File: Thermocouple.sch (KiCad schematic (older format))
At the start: 22 parts, among them P2 CONN_3X2, P3 CONN_2, U2 MCP3901, U3 LMT84, U4 OPA4170

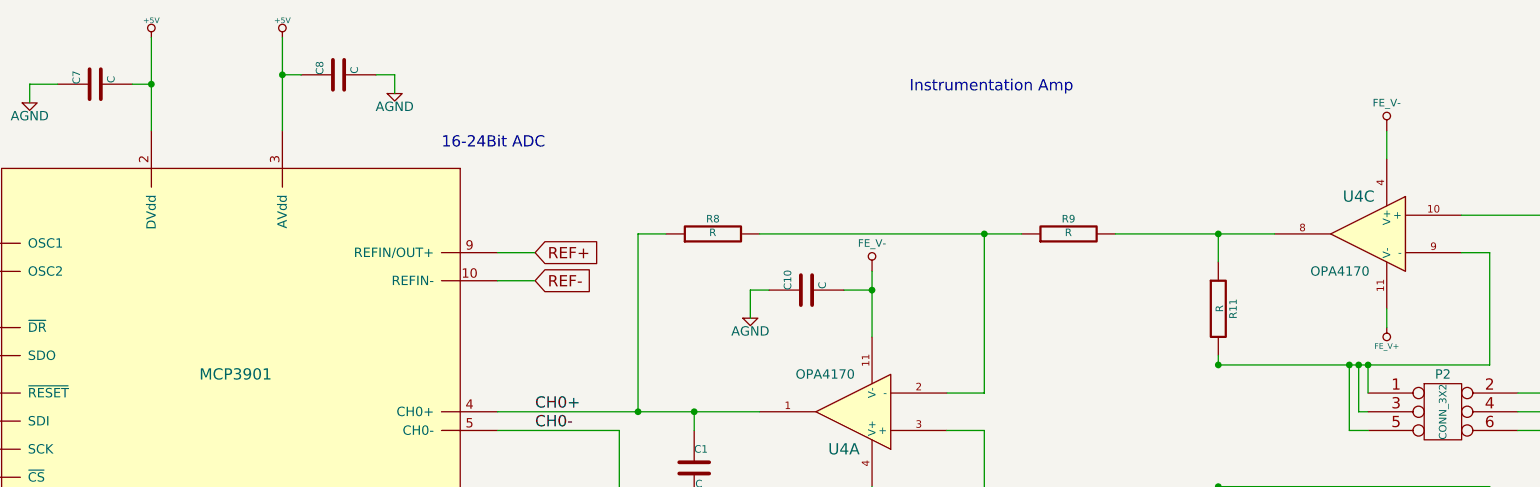
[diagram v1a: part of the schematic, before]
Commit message: Layout Work Session 12
Pulled from CE.

Session 11 missed due to corrupted pcb file pulled from CE
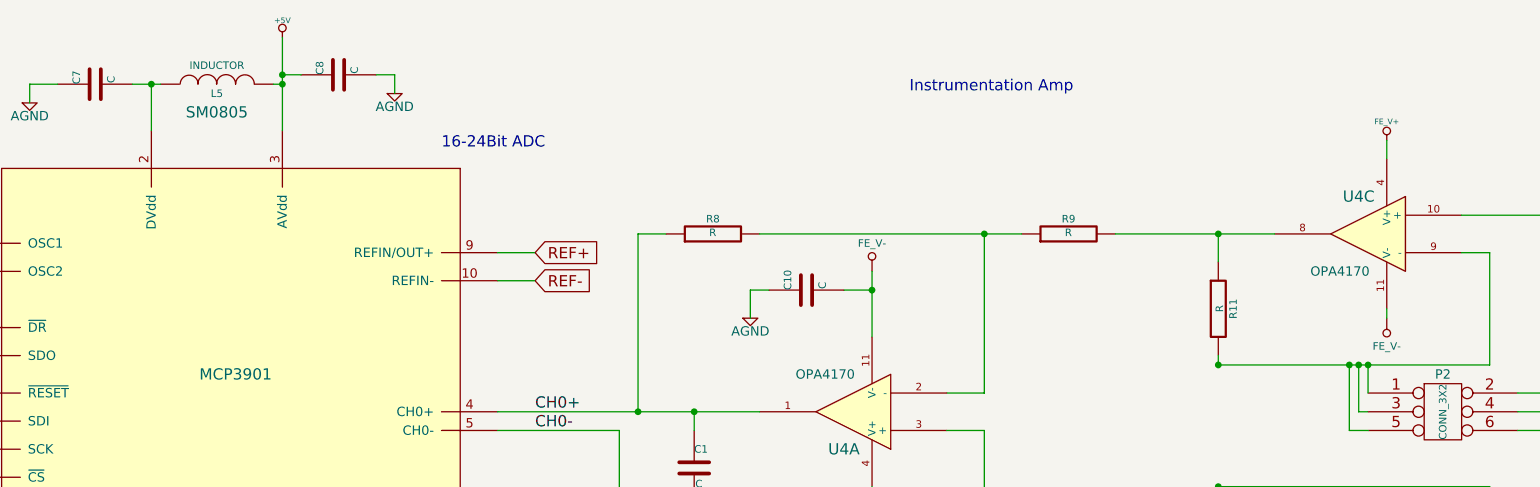
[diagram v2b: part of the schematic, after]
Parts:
- added L5: INDUCTOR, SM0805, symbol INDUCTOR
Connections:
- net +5V: now also L5.2; no longer C7.2, U2.2 (DVdd)
- net FE_V+: now also U4.4 (V+); no longer U4.11 (V-)
- net FE_V-: now also U4.11 (V-); no longer U4.4 (V+)
- new net: C7.2, L5.1, U2.2 (DVdd)
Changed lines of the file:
@@
-EESchema Schematic File Version 2
+EESchema Schematic File Version 2  date 11/21/2013 11:46:41 PM
 LIBS:power
 LIBS:device
@@
 LIBS:BenchBuddy
 LIBS:BenchBuddy-cache
-EELAYER 24 0
+EELAYER 27 0
 EELAYER END
 $Descr A4 11693 8268
@@
 Sheet 2 9
 Title ""
-Date "13 nov 2013"
+Date "22 nov 2013"
 Rev ""
 Comp ""
@@
 	6250 2550 6250 2900
 Wire Wire Line
-	9000 2750 9000 2850
-Wire Wire Line
 	6250 3700 6250 3850
-Wire Wire Line
-	9000 1800 9000 1950
 Wire Wire Line
 	9000 5000 9000 4850
@@
 $EndComp
 Wire Wire Line
-	2400 1300 2400 1800
-Wire Wire Line
-	2400 1550 2300 1550
+	2300 1550 2450 1550
 Connection ~ 2400 1550
 Wire Wire Line
@@
 Wire Wire Line
 	3100 4600 3100 4850
-$Comp
-L +5V #PWR04
-U 1 1 5257AAC2
-P 2400 1300
-F 0 "#PWR04" H 2400 1390 20  0001 C CNN
-F 1 "+5V" H 2400 1390 30  0000 C CNN
-F 2 "~" H 2400 1300 60  0000 C CNN
-F 3 "~" H 2400 1300 60  0000 C CNN
-	1    2400 1300
-	1    0    0    -1
-$EndComp
 Text Notes 6500 6050 0    60   ~ 0
 TEMP SENSOR
@@
 	4550 3900 4550 6050
 $Comp
-L FE_V- #PWR13
+L FE_V- #PWR12
 U 1 1 526E01DB
 P 6250 2550
-F 0 "#PWR13" H 6250 2750 40  0001 C CNN
+F 0 "#PWR12" H 6250 2750 40  0001 C CNN
 F 1 "FE_V-" H 6250 2700 40  0000 C CNN
 F 2 "~" H 6250 2550 60  0000 C CNN
@@
 $EndComp
 $Comp
-L FE_V+ #PWR05
+L FE_V+ #PWR04
 U 1 1 526E01E1
 P 6250 3850
-F 0 "#PWR05" H 6250 3950 30  0001 C CNN
+F 0 "#PWR04" H 6250 3950 30  0001 C CNN
 F 1 "FE_V+" H 6250 3950 30  0000 C CNN
 F 2 "~" H 6250 3850 60  0000 C CNN
@@
 $EndComp
 $Comp
-L FE_V+ #PWR06
+L FE_V+ #PWR05
 U 1 1 526E01F1
 P 9000 5000
-F 0 "#PWR06" H 9000 5100 30  0001 C CNN
+F 0 "#PWR05" H 9000 5100 30  0001 C CNN
 F 1 "FE_V+" H 9000 5100 30  0000 C CNN
 F 2 "~" H 9000 5000 60  0000 C CNN
@@
 $EndComp
 $Comp
-L FE_V- #PWR17
+L FE_V- #PWR16
 U 1 1 526E0201
 P 9000 3950
-F 0 "#PWR17" H 9000 4150 40  0001 C CNN
+F 0 "#PWR16" H 9000 4150 40  0001 C CNN
 F 1 "FE_V-" H 9000 4100 40  0000 C CNN
 F 2 "~" H 9000 3950 60  0000 C CNN
@@
 L FE_V- #PWR15
 U 1 1 526E0207
-P 9000 1800
-F 0 "#PWR15" H 9000 2000 40  0001 C CNN
-F 1 "FE_V-" H 9000 1950 40  0000 C CNN
-F 2 "~" H 9000 1800 60  0000 C CNN
-F 3 "~" H 9000 1800 60  0000 C CNN
-	1    9000 1800
-	1    0    0    -1
-$EndComp
-$Comp
-L FE_V+ #PWR07
+P 9000 2800
+F 0 "#PWR15" H 9000 3000 40  0001 C CNN
+F 1 "FE_V-" H 9000 2950 40  0000 C CNN
+F 2 "~" H 9000 2800 60  0000 C CNN
+F 3 "~" H 9000 2800 60  0000 C CNN
+	1    9000 2800
+	-1   0    0    1
+$EndComp
+$Comp
+L FE_V+ #PWR06
 U 1 1 526E020D
-P 9000 2850
-F 0 "#PWR07" H 9000 2950 30  0001 C CNN
-F 1 "FE_V+" H 9000 2950 30  0000 C CNN
-F 2 "~" H 9000 2850 60  0000 C CNN
-F 3 "~" H 9000 2850 60  0000 C CNN
-	1    9000 2850
-	-1   0    0    1
-$EndComp
-$Comp
-L AGND #PWR08
+P 9000 1850
+F 0 "#PWR06" H 9000 1950 30  0001 C CNN
+F 1 "FE_V+" H 9000 1950 30  0000 C CNN
+F 2 "~" H 9000 1850 60  0000 C CNN
+F 3 "~" H 9000 1850 60  0000 C CNN
+	1    9000 1850
+	1    0    0    -1
+$EndComp
+$Comp
+L AGND #PWR07
 U 1 1 527EEF67
 P 3100 4850
-F 0 "#PWR08" H 3100 4850 40  0001 C CNN
+F 0 "#PWR07" H 3100 4850 40  0001 C CNN
 F 1 "AGND" H 3100 4780 50  0000 C CNN
 F 2 "~" H 3100 4850 60  0000 C CNN
@@
 $EndComp
 $Comp
-L AGND #PWR09
+L AGND #PWR08
 U 1 1 527EEF6D
 P 2300 4850
-F 0 "#PWR09" H 2300 4850 40  0001 C CNN
+F 0 "#PWR08" H 2300 4850 40  0001 C CNN
 F 1 "AGND" H 2300 4780 50  0000 C CNN
 F 2 "~" H 2300 4850 60  0000 C CNN
@@
 $EndComp
 $Comp
-L AGND #PWR010
+L AGND #PWR09
 U 1 1 527EEF73
 P 1750 1650
-F 0 "#PWR010" H 1750 1650 40  0001 C CNN
+F 0 "#PWR09" H 1750 1650 40  0001 C CNN
 F 1 "AGND" H 1750 1580 50  0000 C CNN
 F 2 "~" H 1750 1650 60  0000 C CNN
@@
 $EndComp
 $Comp
-L AGND #PWR011
+L AGND #PWR010
 U 1 1 527EEF79
 P 3700 1600
-F 0 "#PWR011" H 3700 1600 40  0001 C CNN
+F 0 "#PWR010" H 3700 1600 40  0001 C CNN
 F 1 "AGND" H 3700 1530 50  0000 C CNN
 F 2 "~" H 3700 1600 60  0000 C CNN
@@
 $EndComp
 $Comp
-L AGND #PWR012
+L AGND #PWR011
 U 1 1 527EEF7F
 P 5600 2800
-F 0 "#PWR012" H 5600 2800 40  0001 C CNN
+F 0 "#PWR011" H 5600 2800 40  0001 C CNN
 F 1 "AGND" H 5600 2730 50  0000 C CNN
 F 2 "~" H 5600 2800 60  0000 C CNN
@@
 $EndComp
 $Comp
-L AGND #PWR013
+L AGND #PWR012
 U 1 1 527EEF85
 P 5550 4000
-F 0 "#PWR013" H 5550 4000 40  0001 C CNN
+F 0 "#PWR012" H 5550 4000 40  0001 C CNN
 F 1 "AGND" H 5550 3930 50  0000 C CNN
 F 2 "~" H 5550 4000 60  0000 C CNN
@@
 $EndComp
 $Comp
-L AGND #PWR014
+L AGND #PWR013
 U 1 1 527EEF8B
 P 4900 4700
-F 0 "#PWR014" H 4900 4700 40  0001 C CNN
+F 0 "#PWR013" H 4900 4700 40  0001 C CNN
 F 1 "AGND" H 4900 4630 50  0000 C CNN
 F 2 "~" H 4900 4700 60  0000 C CNN
@@
 $EndComp
 $Comp
-L AGND #PWR015
+L AGND #PWR014
 U 1 1 527EEF91
 P 4800 6900
-F 0 "#PWR015" H 4800 6900 40  0001 C CNN
+F 0 "#PWR014" H 4800 6900 40  0001 C CNN
 F 1 "AGND" H 4800 6830 50  0000 C CNN
 F 2 "~" H 4800 6900 60  0000 C CNN
@@
 	1    0    0    -1
 $EndComp
+Wire Wire Line
+	9000 2800 9000 2750
+Wire Wire Line
+	9000 1850 9000 1950
+Wire Wire Line
+	2400 1550 2400 1800
+$Comp
+L INDUCTOR L5
+U 1 1 528976A6
+P 2750 1550
+F 0 "L5" V 2700 1550 40  0000 C CNN
+F 1 "INDUCTOR" V 2850 1550 40  0000 C CNN
+F 2 "SM0805" V 2600 1550 60  0000 C CNN
+F 3 "~" H 2750 1550 60  0000 C CNN
+	1    2750 1550
+	0    -1   -1   0
+$EndComp
+Wire Wire Line
+	3050 1550 3100 1550
+Connection ~ 3100 1550
 $EndSCHEMATC

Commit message: Layout Work Session 14
Pulled from CE
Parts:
- added C30, C31: C, SM0805, symbol C
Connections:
- net at U2.15 (OSC1): now also C30.2
- net at U2.16 (OSC2): now also C30.1
- net REF+: no longer names the net of U2.9 (REFIN/OUT+)
- net REF+: now also C31.2
- net REF-: no longer names the net of U2.10 (REFIN-)
- net REF-: now also C31.1
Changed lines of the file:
@@
-EESchema Schematic File Version 2  date 11/21/2013 11:46:41 PM
+EESchema Schematic File Version 2  date 11/24/2013 3:13:43 PM
 LIBS:power
 LIBS:device
@@
 Sheet 2 9
 Title ""
-Date "22 nov 2013"
+Date "24 nov 2013"
 Rev ""
 Comp ""
@@
 Connection ~ 4800 6800
 $Comp
-L +5V #PWR01
+L +5V #PWR10
 U 1 1 5257A1D1
 P 5600 5000
-F 0 "#PWR01" H 5600 5090 20  0001 C CNN
+F 0 "#PWR10" H 5600 5090 20  0001 C CNN
 F 1 "+5V" H 5600 5090 30  0000 C CNN
 F 2 "~" H 5600 5000 60  0000 C CNN
@@
 	6050 3800 6250 3800
 $Comp
-L +5V #PWR02
+L +5V #PWR11
 U 1 1 5257A5A4
 P 5600 5000
-F 0 "#PWR02" H 5600 5090 20  0001 C CNN
+F 0 "#PWR11" H 5600 5090 20  0001 C CNN
 F 1 "+5V" H 5600 5090 30  0000 C CNN
 F 2 "~" H 5600 5000 60  0000 C CNN
@@
 $EndComp
 $Comp
-L +5V #PWR03
+L +5V #PWR3
 U 1 1 5257A5AA
 P 3100 1300
-F 0 "#PWR03" H 3100 1390 20  0001 C CNN
+F 0 "#PWR3" H 3100 1390 20  0001 C CNN
 F 1 "+5V" H 3100 1390 30  0000 C CNN
 F 2 "~" H 3100 1300 60  0000 C CNN
@@
 Wire Wire Line
 	3100 1300 3100 1800
-Text GLabel 4450 2450 2    60   Input ~ 0
-REF+
-Text GLabel 4450 2600 2    60   Input ~ 0
-REF-
 Wire Wire Line
 	4450 2600 4250 2600
@@
 $EndComp
 $Comp
-L FE_V+ #PWR04
+L FE_V+ #PWR13
 U 1 1 526E01E1
 P 6250 3850
-F 0 "#PWR04" H 6250 3950 30  0001 C CNN
+F 0 "#PWR13" H 6250 3950 30  0001 C CNN
 F 1 "FE_V+" H 6250 3950 30  0000 C CNN
 F 2 "~" H 6250 3850 60  0000 C CNN
@@
 $EndComp
 $Comp
-L FE_V+ #PWR05
+L FE_V+ #PWR17
 U 1 1 526E01F1
 P 9000 5000
-F 0 "#PWR05" H 9000 5100 30  0001 C CNN
+F 0 "#PWR17" H 9000 5100 30  0001 C CNN
 F 1 "FE_V+" H 9000 5100 30  0000 C CNN
 F 2 "~" H 9000 5000 60  0000 C CNN
@@
 $EndComp
 $Comp
-L FE_V+ #PWR06
+L FE_V+ #PWR14
 U 1 1 526E020D
 P 9000 1850
-F 0 "#PWR06" H 9000 1950 30  0001 C CNN
+F 0 "#PWR14" H 9000 1950 30  0001 C CNN
 F 1 "FE_V+" H 9000 1950 30  0000 C CNN
 F 2 "~" H 9000 1850 60  0000 C CNN
@@
 $EndComp
 $Comp
-L AGND #PWR07
+L AGND #PWR4
 U 1 1 527EEF67
 P 3100 4850
-F 0 "#PWR07" H 3100 4850 40  0001 C CNN
+F 0 "#PWR4" H 3100 4850 40  0001 C CNN
 F 1 "AGND" H 3100 4780 50  0000 C CNN
 F 2 "~" H 3100 4850 60  0000 C CNN
@@
 $EndComp
 $Comp
-L AGND #PWR08
+L AGND #PWR2
 U 1 1 527EEF6D
 P 2300 4850
-F 0 "#PWR08" H 2300 4850 40  0001 C CNN
+F 0 "#PWR2" H 2300 4850 40  0001 C CNN
 F 1 "AGND" H 2300 4780 50  0000 C CNN
 F 2 "~" H 2300 4850 60  0000 C CNN
@@
 $EndComp
 $Comp
-L AGND #PWR09
+L AGND #PWR1
 U 1 1 527EEF73
 P 1750 1650
-F 0 "#PWR09" H 1750 1650 40  0001 C CNN
+F 0 "#PWR1" H 1750 1650 40  0001 C CNN
 F 1 "AGND" H 1750 1580 50  0000 C CNN
 F 2 "~" H 1750 1650 60  0000 C CNN
@@
 $EndComp
 $Comp
-L AGND #PWR010
+L AGND #PWR5
 U 1 1 527EEF79
 P 3700 1600
-F 0 "#PWR010" H 3700 1600 40  0001 C CNN
+F 0 "#PWR5" H 3700 1600 40  0001 C CNN
 F 1 "AGND" H 3700 1530 50  0000 C CNN
 F 2 "~" H 3700 1600 60  0000 C CNN
@@
 $EndComp
 $Comp
-L AGND #PWR011
+L AGND #PWR9
 U 1 1 527EEF7F
 P 5600 2800
-F 0 "#PWR011" H 5600 2800 40  0001 C CNN
+F 0 "#PWR9" H 5600 2800 40  0001 C CNN
 F 1 "AGND" H 5600 2730 50  0000 C CNN
 F 2 "~" H 5600 2800 60  0000 C CNN
@@
 $EndComp
 $Comp
-L AGND #PWR012
+L AGND #PWR8
 U 1 1 527EEF85
 P 5550 4000
-F 0 "#PWR012" H 5550 4000 40  0001 C CNN
+F 0 "#PWR8" H 5550 4000 40  0001 C CNN
 F 1 "AGND" H 5550 3930 50  0000 C CNN
 F 2 "~" H 5550 4000 60  0000 C CNN
@@
 $EndComp
 $Comp
-L AGND #PWR013
+L AGND #PWR7
 U 1 1 527EEF8B
 P 4900 4700
-F 0 "#PWR013" H 4900 4700 40  0001 C CNN
+F 0 "#PWR7" H 4900 4700 40  0001 C CNN
 F 1 "AGND" H 4900 4630 50  0000 C CNN
 F 2 "~" H 4900 4700 60  0000 C CNN
@@
 $EndComp
 $Comp
-L AGND #PWR014
+L AGND #PWR6
 U 1 1 527EEF91
 P 4800 6900
-F 0 "#PWR014" H 4800 6900 40  0001 C CNN
+F 0 "#PWR6" H 4800 6900 40  0001 C CNN
 F 1 "AGND" H 4800 6830 50  0000 C CNN
 F 2 "~" H 4800 6900 60  0000 C CNN
@@
 	3050 1550 3100 1550
 Connection ~ 3100 1550
+$Comp
+L C C30
+U 1 1 529268AF
+P 1000 2450
+F 0 "C30" H 1000 2550 40  0000 L CNN
+F 1 "C" H 1006 2365 40  0000 L CNN
+F 2 "SM0805" H 1038 2300 30  0000 C CNN
+F 3 "~" H 1000 2450 60  0000 C CNN
+	1    1000 2450
+	-1   0    0    1
+$EndComp
+Wire Wire Line
+	1000 2250 1250 2250
+Wire Wire Line
+	1250 2250 1250 2400
+Wire Wire Line
+	1250 2400 1400 2400
+Wire Wire Line
+	1400 2550 1250 2550
+Wire Wire Line
+	1250 2550 1250 2700
+Wire Wire Line
+	1250 2700 1000 2700
+Wire Wire Line
+	1000 2700 1000 2650
+$Comp
+L C C31
+U 1 1 52926A41
+P 4800 2500
+F 0 "C31" H 4800 2600 40  0000 L CNN
+F 1 "C" H 4806 2415 40  0000 L CNN
+F 2 "SM0805" H 4838 2350 30  0000 C CNN
+F 3 "~" H 4800 2500 60  0000 C CNN
+	1    4800 2500
+	-1   0    0    1
+$EndComp
+Wire Wire Line
+	4800 2300 4800 2200
+Wire Wire Line
+	4800 2200 4450 2200
+Wire Wire Line
+	4450 2200 4450 2450
+Wire Wire Line
+	4450 2600 4450 2900
+Wire Wire Line
+	4450 2900 4800 2900
+Wire Wire Line
+	4800 2900 4800 2700
 $EndSCHEMATC
